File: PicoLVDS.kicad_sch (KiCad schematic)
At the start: 10 parts, among them J1 Conn_02x16, U1 Pico, U2 SN65LVDS047D, U3 SN65LVDS047D, U4 SN65LVDS047D, U5 SN65LVDS047D

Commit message: v2
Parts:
- removed U2, U3, U4, U5: SN65LVDS047D, Package_SO:SOIC-16_3.9x9.9mm_P1.27mm, symbol Interface:SN65LVDS047D
- added U2, U3, U4, U5: SN65LVDS391D, Package_SO:SOIC-16_3.9x9.9mm_P1.27mm, symbol Kria_Board_Parts:SN65LVDS391D
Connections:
- net +3V3: now also U2.1 (EN1,2), U2.4 (VCC), U2.8 (EN3,4), U3.1 (EN1,2), U3.4 (VCC), U3.8 (EN3,4), U4.1 (EN1,2), U4.4 (VCC), U4.8 (EN3,4), U5.1 (EN1,2), U5.4 (VCC), U5.8 (EN3,4)
- net D0: now also U2.7 (DIN4)
- net D1: now also U2.6 (DIN3)
- net D10: now also U4.3 (DIN2)
- net D11: now also U4.2 (DIN1)
- net D12: now also U5.7 (DIN4)
- net D13: now also U5.6 (DIN3)
- net D14: now also U5.3 (DIN2)
- net D15: now also U5.2 (DIN1)
- net D2: now also U2.3 (DIN2)
- net D3: now also U2.2 (DIN1)
- net D4: now also U3.7 (DIN4)
- net D5: now also U3.6 (DIN3)
- net D6: now also U3.3 (DIN2)
- net D7: now also U3.2 (DIN1)
- net D8: now also U4.7 (DIN4)
- net D9: now also U4.6 (DIN3)
- net GND: now also U2.5 (GND), U3.5 (GND), U4.5 (GND), U5.5 (GND)
- net Out_0+: now also U2.10 (DOUT4+)
- net Out_0-: now also U2.9 (DOUT4-)
- net Out_1+: now also U2.12 (DOUT3+)
- net Out_1-: now also U2.11 (DOUT3-)
- net Out_10+: now also U4.14 (DOUT2+)
- net Out_10-: now also U4.13 (DOUT2-)
- net Out_11+: now also U4.16 (DOUT1+)
- net Out_11-: now also U4.15 (DOUT1-)
- net Out_12+: now also U5.10 (DOUT4+)
- net Out_12-: now also U5.9 (DOUT4-)
- net Out_13+: now also U5.12 (DOUT3+)
- net Out_13-: now also U5.11 (DOUT3-)
- net Out_14+: now also U5.14 (DOUT2+)
- net Out_14-: now also U5.13 (DOUT2-)
- net Out_15+: now also U5.16 (DOUT1+)
- net Out_15-: now also U5.15 (DOUT1-)
- net Out_2+: now also U2.14 (DOUT2+)
- net Out_2-: now also U2.13 (DOUT2-)
- net Out_3+: now also U2.16 (DOUT1+)
- net Out_3-: now also U2.15 (DOUT1-)
- net Out_4+: now also U3.10 (DOUT4+)
- net Out_4-: now also U3.9 (DOUT4-)
- net Out_5+: now also U3.12 (DOUT3+)
- net Out_5-: now also U3.11 (DOUT3-)
- net Out_6+: now also U3.14 (DOUT2+)
- net Out_6-: now also U3.13 (DOUT2-)
- net Out_7+: now also U3.16 (DOUT1+)
- net Out_7-: now also U3.15 (DOUT1-)
- net Out_8+: now also U4.10 (DOUT4+)
- net Out_8-: now also U4.9 (DOUT4-)
- net Out_9+: now also U4.12 (DOUT3+)
- net Out_9-: now also U4.11 (DOUT3-)
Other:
- moved on the sheet: J1

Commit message: Schematic v2
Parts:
- added C5, C6, C7, C8: C100n, Capacitor_SMD:C_0402_1005Metric_Pad0.74x0.62mm_HandSolder, symbol Device:C
- added J2: RJHSE508002, RJHSE508002:AMPHENOL_RJHSE508002, symbol RJHSE508002:RJHSE508002
- added U10, U11, U8, U9: SN65MLVD206BD, D0008A_N, symbol SN65MLVD206BD:SN65MLVD206BD
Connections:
- net +3V3: now also C5.1, C6.1, C7.1, C8.1, U10.8 (VCC), U11.8 (VCC), U8.8 (VCC), U9.8 (VCC)
- net GND: now also C5.2, C6.2, C7.2, C8.2, U10.5 (GND), U11.5 (GND), U8.5 (GND), U9.5 (GND)
- net D16: now reaches U1.21 (GPIO16)
- net D16: now also U10.1 (R), U10.4 (D)
- net D17: now reaches U1.22 (GPIO17)
- net D17: now also U11.1 (R), U11.4 (D)
- net D18: now reaches U1.24 (GPIO18)
- net D18: now also U8.1 (R), U8.4 (D)
- net D19: now reaches U1.25 (GPIO19)
- net D19: now also U9.1 (R), U9.4 (D)
- net SR: now reaches U1.26 (GPIO20)
- net SR: now also U10.2 (RE_N), U10.3 (DE), U11.2 (RE_N), U11.3 (DE), U8.2 (RE_N), U8.3 (DE), U9.2 (RE_N), U9.3 (DE)
- new net Out_16+: J2.1_1, J2.2_1, U10.6 (A)
- new net Out_16-: J2.1_2, J2.2_2, U10.7 (B)
- new net Out_17+: J2.1_3, J2.2_3, U11.6 (A)
- new net Out_17-: J2.1_6, J2.2_6, U11.7 (B)
- new net Out_18+: J2.1_4, J2.2_4, U8.6 (A)
- new net Out_18-: J2.1_5, J2.2_5, U8.7 (B)
- new net Out_19+: J2.1_7, J2.2_7, U9.6 (A)
- new net Out_19-: J2.1_8, J2.2_8, U9.7 (B)
- no-connect marks 21 -> 16
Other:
- moved on the sheet: C1, C2, C3, C4, J1, U2, U3, U4, U5

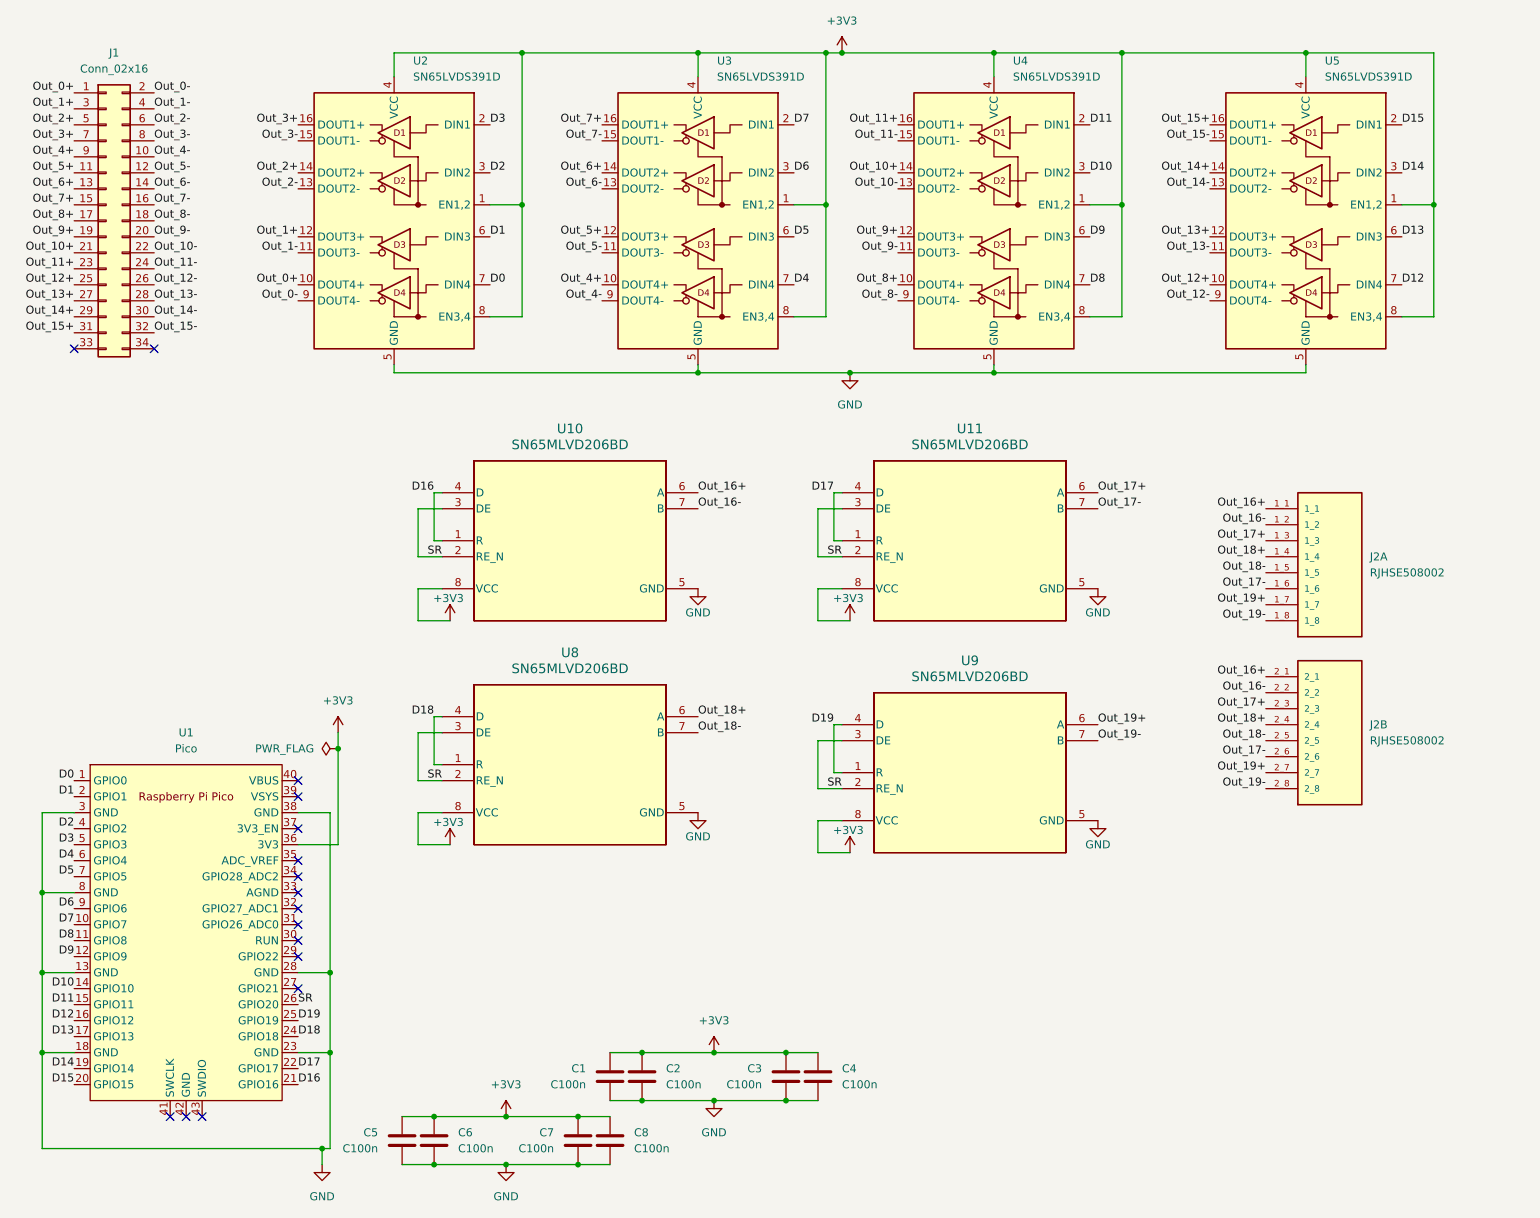
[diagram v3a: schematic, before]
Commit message: Switch to SMT footprint
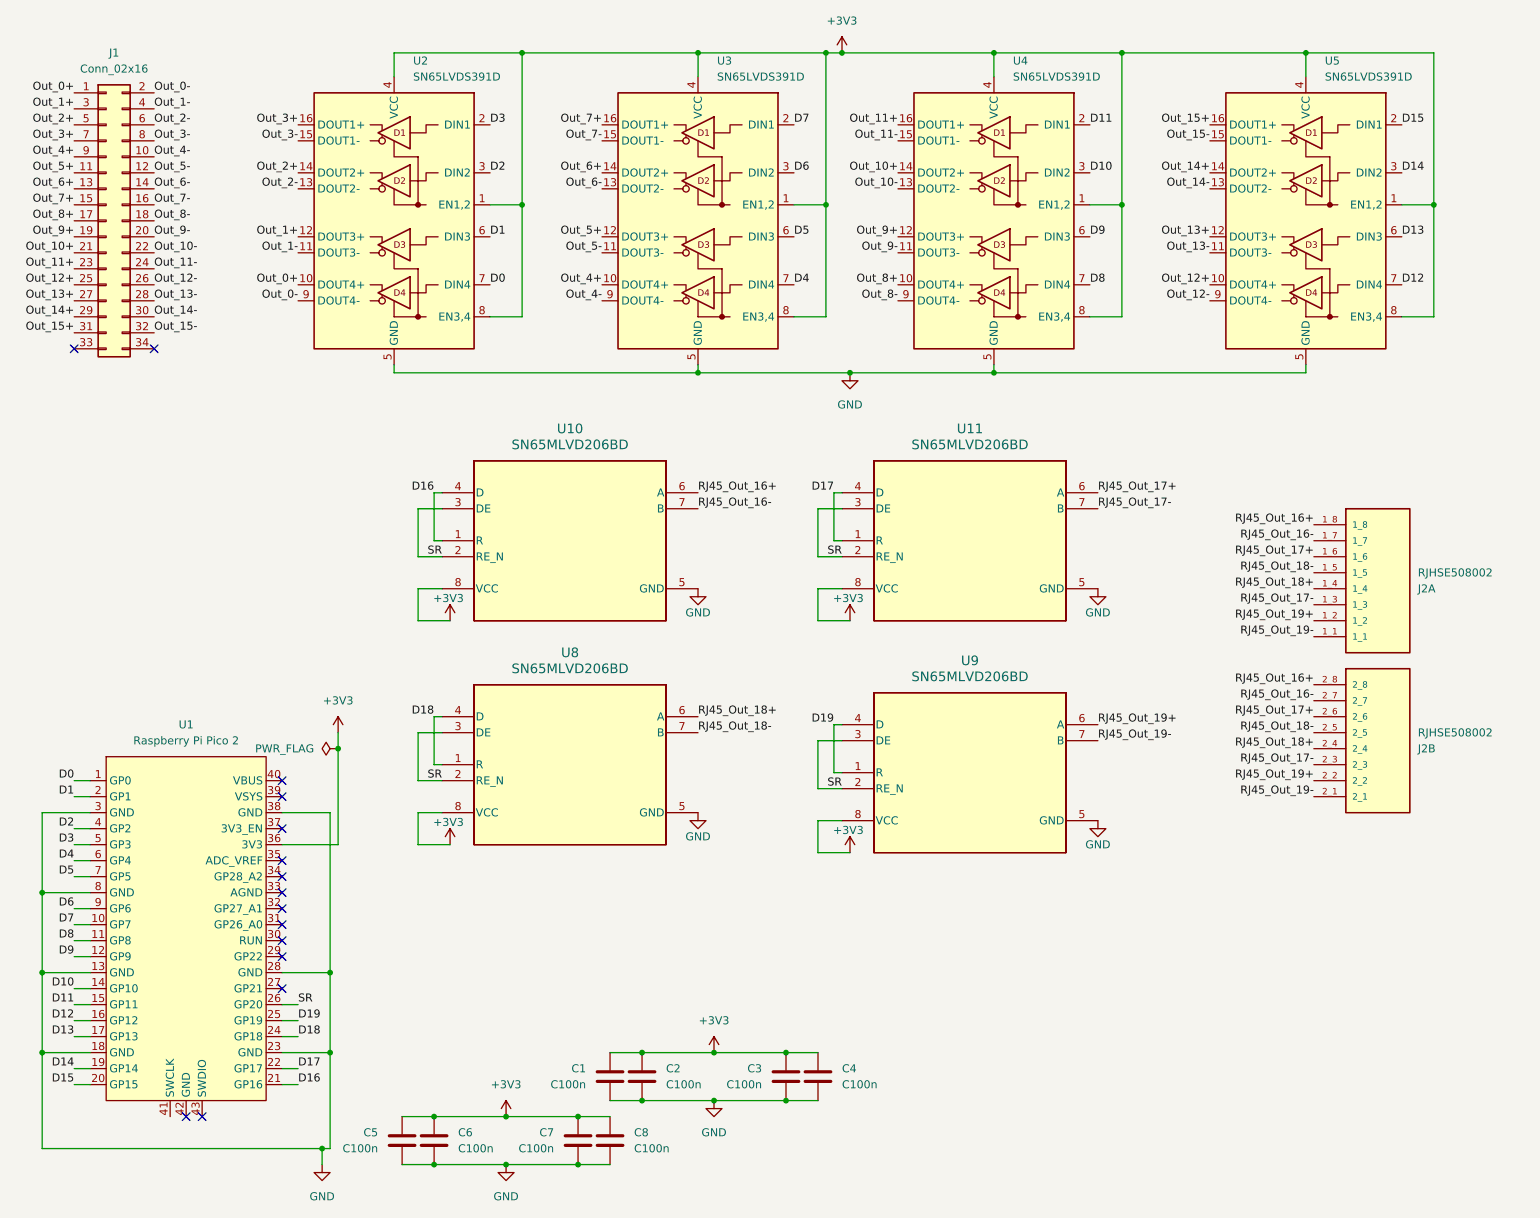
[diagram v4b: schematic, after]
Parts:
- removed U1: Pico, RPi_Pico:RPi_Pico_SMD_TH, symbol MCU_RaspberryPi_and_Boards:Pico
- added U1: Raspberry Pi Pico 2, RasPi_Pico:RasPi_Pico_2_SMD, symbol RasPi_Pico:Raspberry_Pi_Pico_2
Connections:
- net +3V3: now also U1.36 (3V3)
- net D0: now also U1.1 (GP0)
- net D1: now also U1.2 (GP1)
- net D10: now also U1.14 (GP10)
- net D11: now also U1.15 (GP11)
- net D12: now also U1.16 (GP12)
- net D13: now also U1.17 (GP13)
- net D14: now also U1.19 (GP14)
- net D15: now also U1.20 (GP15)
- net D16: now also U1.21 (GP16)
- net D17: now also U1.22 (GP17)
- net D18: now also U1.24 (GP18)
- net D19: now also U1.25 (GP19)
- net D2: now also U1.4 (GP2)
- net D3: now also U1.5 (GP3)
- net D4: now also U1.6 (GP4)
- net D5: now also U1.7 (GP5)
- net D6: now also U1.9 (GP6)
- net D7: now also U1.10 (GP7)
- net D8: now also U1.11 (GP8)
- net D9: now also U1.12 (GP9)
- net GND: now also U1.13 (GND), U1.18 (GND), U1.23 (GND), U1.28 (GND), U1.3 (GND), U1.38 (GND), U1.8 (GND)
- net SR: now also U1.26 (GP20)
- net Out_16+ renamed RJ45_Out_19-
- net RJ45_Out_19-: now also U9.7 (B); no longer U10.6 (A)
- net Out_16- renamed RJ45_Out_19+
- net RJ45_Out_19+: now also U9.6 (A); no longer U10.7 (B)
- net Out_17+ renamed RJ45_Out_17-
- net RJ45_Out_17-: now also U11.7 (B); no longer U11.6 (A)
- net Out_17- renamed RJ45_Out_17+
- net RJ45_Out_17+: now also U11.6 (A); no longer U11.7 (B)
- net Out_18+ renamed RJ45_Out_18+
- net Out_18- renamed RJ45_Out_18-
- net Out_19+ renamed RJ45_Out_16-
- net RJ45_Out_16-: now also U10.7 (B); no longer U9.6 (A)
- net Out_19- renamed RJ45_Out_16+
- net RJ45_Out_16+: now also U10.6 (A); no longer U9.7 (B)
- no-connect marks 16 -> 15
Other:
- moved on the sheet: J2B
